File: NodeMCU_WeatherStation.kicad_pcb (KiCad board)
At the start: 2 copper layers, 64 x 90 mm, 98 parts, among them J1 AVR-ISP-6, J10 Screw_Terminal_01x03, J11 Screw_Terminal_01x03, J12 Screw_Terminal_01x02, J13 Screw_Terminal_01x02, J14 Screw_Terminal_01x02, J15 Conn_01x10, J2 Conn_01x15, J3 Conn_01x15, J4 Conn_01x04, J5 Conn_01x04, J6 Conn_01x15, J7 Conn_01x15, J8 Conn_01x07, J9 Screw_Terminal_01x04, U1 BME280, U2 ATmega328P-AU, U3 TLC555CD, U4 ADS122C04IPW, U5 LT1492, U6 LT1492, U7 R-785.0-0.5, Y1 16MHz

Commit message: cleaned up PCB labels
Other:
- board text added: "AVR ISP"
- board text added: "IN1"
- board text added: "IN2"
- board text added: "NodeMCU Weather Station"
- board text added: "OUT1"
- board text added: "OUT2"
- board text added: "RXD"
- board text added: "TXD"
- board text added: "Water Level"
- board text removed: "NodeMCU Wheather Station"
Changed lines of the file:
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@@
   (general
     (thickness 1.6)
-    (drawings 33)
+    (drawings 50)
     (tracks 785)
     (zones 0)
@@
   (page A4)
   (layers
-    (0 F.Cu signal)
-    (31 B.Cu signal)
-    (32 B.Adhes user)
+    (0 F.Cu signal hide)
+    (31 B.Cu signal hide)
+    (32 B.Adhes user hide)
     (33 F.Adhes user)
-    (34 B.Paste user)
+    (34 B.Paste user hide)
     (35 F.Paste user)
-    (36 B.SilkS user)
+    (36 B.SilkS user hide)
     (37 F.SilkS user)
-    (38 B.Mask user)
+    (38 B.Mask user hide)
     (39 F.Mask user)
     (40 Dwgs.User user)
@@
     (44 Edge.Cuts user)
     (45 Margin user)
-    (46 B.CrtYd user)
-    (47 F.CrtYd user)
-    (48 B.Fab user)
-    (49 F.Fab user)
+    (46 B.CrtYd user hide)
+    (47 F.CrtYd user hide)
+    (48 B.Fab user hide)
+    (49 F.Fab user hide)
   )
   (setup
@@
     (descr "terminal block Metz Connect Type055_RT01502HDWU, 2 pins, pitch 5mm, size 10x8mm^2, drill diamater 1.3mm, pad diameter 2.5mm, see http://www.metz-connect.com/de/system/files/productfiles/Datenblatt_310551_RT015xxHDWU_OFF-022723S.pdf, script-generated using https://github.com/pointhi/kicad-footprint-generator/scripts/TerminalBlock_MetzConnect")
     (tags "THT terminal block Metz Connect Type055_RT01502HDWU pitch 5mm size 10x8mm^2 drill 1.3mm pad 2.5mm")
-    (fp_text reference J14 (at 2.5 -5.06 90) (layer F.SilkS)
+    (fp_text reference J14 (at -3.81 2.794 180) (layer F.SilkS)
       (effects (font (size 1 1) (thickness 0.15)))
     )
@@
     (descr "DCDC-Converter, RECOM, RECOM_R-78E-0.5, SIP-3, pitch 2.54mm, package size 11.6x8.5x10.4mm^3, https://www.recom-power.com/pdf/Innoline/R-78Exx-0.5.pdf")
     (tags "dc-dc recom buck sip-3 pitch 2.54mm")
-    (fp_text reference U7 (at 2.54 -7.56 90) (layer F.SilkS)
+    (fp_text reference U7 (at -4.1656 -0.3556) (layer F.SilkS)
       (effects (font (size 1 1) (thickness 0.15)))
     )
@@
     (descr "PhotoDiode, plastic DIL, 4.3x4.65mm², RM5.08")
     (tags "PhotoDiode plastic DIL RM5.08")
-    (fp_text reference D7 (at 2.54 -3.17 90) (layer F.SilkS)
+    (fp_text reference D7 (at -0.8128 2.1336 180) (layer F.SilkS)
       (effects (font (size 1 1) (thickness 0.15)))
     )
@@
     (descr "Through hole straight IDC box header, 2x03, 2.54mm pitch, double rows")
     (tags "Through hole IDC box header THT 2x03 2.54mm double row")
-    (fp_text reference J1 (at 1.27 -6.604) (layer F.SilkS)
+    (fp_text reference J1 (at 1.27 -6.604) (layer F.SilkS) hide
       (effects (font (size 1 1) (thickness 0.15)))
     )
@@
     (tags "mounting hole 4.3mm m4")
     (attr virtual)
-    (fp_text reference H5 (at 0 -5.3) (layer F.SilkS)
+    (fp_text reference H5 (at 0 -5.3) (layer F.SilkS) hide
       (effects (font (size 1 1) (thickness 0.15)))
     )
-    (fp_text value MountingHole_Pad (at 0 5.3) (layer F.Fab)
+    (fp_text value MountingHole_Pad (at 0 5.3) (layer F.Fab) hide
       (effects (font (size 1 1) (thickness 0.15)))
     )
     (fp_circle (center 0 0) (end 4.55 0) (layer F.CrtYd) (width 0.05))
     (fp_circle (center 0 0) (end 4.3 0) (layer Cmts.User) (width 0.15))
-    (fp_text user %R (at 0.3 0) (layer F.Fab)
+    (fp_text user %R (at 0.3 0) (layer F.Fab) hide
       (effects (font (size 1 1) (thickness 0.15)))
     )
@@
     (tags "mounting hole 4.3mm m4")
     (attr virtual)
-    (fp_text reference H4 (at 0 -5.3) (layer F.SilkS)
+    (fp_text reference H4 (at 0 -5.3) (layer F.SilkS) hide
       (effects (font (size 1 1) (thickness 0.15)))
     )
-    (fp_text value MountingHole_Pad (at 0 5.3) (layer F.Fab)
+    (fp_text value MountingHole_Pad (at 0 5.3) (layer F.Fab) hide
       (effects (font (size 1 1) (thickness 0.15)))
     )
     (fp_circle (center 0 0) (end 4.55 0) (layer F.CrtYd) (width 0.05))
     (fp_circle (center 0 0) (end 4.3 0) (layer Cmts.User) (width 0.15))
-    (fp_text user %R (at 0.3 0) (layer F.Fab)
+    (fp_text user %R (at 0.3 0) (layer F.Fab) hide
       (effects (font (size 1 1) (thickness 0.15)))
     )
@@
     (tags "mounting hole 4.3mm m4")
     (attr virtual)
-    (fp_text reference H2 (at 5.1308 -3.386) (layer F.SilkS)
+    (fp_text reference H2 (at 5.1308 -3.386) (layer F.SilkS) hide
       (effects (font (size 1 1) (thickness 0.15)))
     )
-    (fp_text value MountingHole_Pad (at 0 5.3) (layer F.Fab)
+    (fp_text value MountingHole_Pad (at 0 5.3) (layer F.Fab) hide
       (effects (font (size 1 1) (thickness 0.15)))
     )
-    (fp_text user %R (at 0.3 0) (layer F.Fab)
+    (fp_text user %R (at 0.3 0) (layer F.Fab) hide
       (effects (font (size 1 1) (thickness 0.15)))
     )
@@
     (tags "mounting hole 4.3mm m4")
     (attr virtual)
-    (fp_text reference H1 (at -5.09 -3.386) (layer F.SilkS)
+    (fp_text reference H1 (at -5.09 -3.386) (layer F.SilkS) hide
       (effects (font (size 1 1) (thickness 0.15)))
     )
-    (fp_text value MountingHole_Pad (at 0 5.3) (layer F.Fab)
+    (fp_text value MountingHole_Pad (at 0 5.3) (layer F.Fab) hide
       (effects (font (size 1 1) (thickness 0.15)))
     )
-    (fp_text user %R (at 0.3 0) (layer F.Fab)
+    (fp_text user %R (at 0.3 0) (layer F.Fab) hide
       (effects (font (size 1 1) (thickness 0.15)))
     )
@@
     )
   )
+  (gr_text "Water Level" (at 86.8504 140.6552) (layer F.SilkS)
+    (effects (font (size 1 1) (thickness 0.15)))
+  )
+  (gr_text +5V (at 119.464 63.0328) (layer F.SilkS)
+    (effects (font (size 1 1) (thickness 0.15)))
+  )
+  (gr_text GND (at 119.6164 58.1052) (layer F.SilkS)
+    (effects (font (size 1 1) (thickness 0.15)))
+  )
+  (gr_text "AVR ISP" (at 111.0312 140.9092) (layer F.SilkS)
+    (effects (font (size 1 1) (thickness 0.15)))
+  )
+  (gr_text GND (at 124.039181 85.4356) (layer F.SilkS)
+    (effects (font (size 1 1) (thickness 0.15)))
+  )
+  (gr_text RXD (at 124.0868 80.4572) (layer F.SilkS)
+    (effects (font (size 1 1) (thickness 0.15)))
+  )
+  (gr_text OUT1 (at 123.756648 124.2976) (layer F.SilkS)
+    (effects (font (size 1 1) (thickness 0.15)))
+  )
+  (gr_text OUT2 (at 123.756648 119.2176) (layer F.SilkS)
+    (effects (font (size 1 1) (thickness 0.15)))
+  )
+  (gr_text IN1 (at 124.423315 114.1376) (layer F.SilkS)
+    (effects (font (size 1 1) (thickness 0.15)))
+  )
+  (gr_text IN2 (at 124.423315 109.0576) (layer F.SilkS)
+    (effects (font (size 1 1) (thickness 0.15)))
+  )
+  (gr_text GND (at 124.1376 121.7576) (layer F.SilkS)
+    (effects (font (size 1 1) (thickness 0.15)))
+  )
+  (gr_text GND (at 124.1376 116.6776) (layer F.SilkS)
+    (effects (font (size 1 1) (thickness 0.15)))
+  )
+  (gr_text GND (at 124.1376 111.5976) (layer F.SilkS)
+    (effects (font (size 1 1) (thickness 0.15)))
+  )
+  (gr_text GND (at 124.1376 106.5176) (layer F.SilkS)
+    (effects (font (size 1 1) (thickness 0.15)))
+  )
+  (gr_text +5V (at 124.1376 103.9776) (layer F.SilkS)
+    (effects (font (size 1 1) (thickness 0.15)))
+  )
+  (gr_text +5V (at 124.1376 101.4376) (layer F.SilkS)
+    (effects (font (size 1 1) (thickness 0.15)))
+  )
+  (gr_text TXD (at 124.205848 82.9464) (layer F.SilkS)
+    (effects (font (size 1 1) (thickness 0.15)))
+  )
   (gr_text PT100 (at 76.9444 48.3516) (layer Dwgs.User)
     (effects (font (size 1 1) (thickness 0.15)))
@@
     (effects (font (size 1.5 1.5) (thickness 0.25)))
   )
-  (gr_text "NodeMCU Wheather Station" (at 126.6776 113.3248 90) (layer F.SilkS)
+  (gr_text "NodeMCU Weather Station" (at 120.6832 111.9024 90) (layer F.SilkS)
     (effects (font (size 1.5 1.5) (thickness 0.25)))
   )

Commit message: changed to 3.2mm holes for mounting the PCB
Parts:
- H3, H4, H5, H6: footprint MountingHole:MountingHole_4.3mm_M4_Pad_Via -> MountingHole:MountingHole_3.2mm_M3_Pad_Via

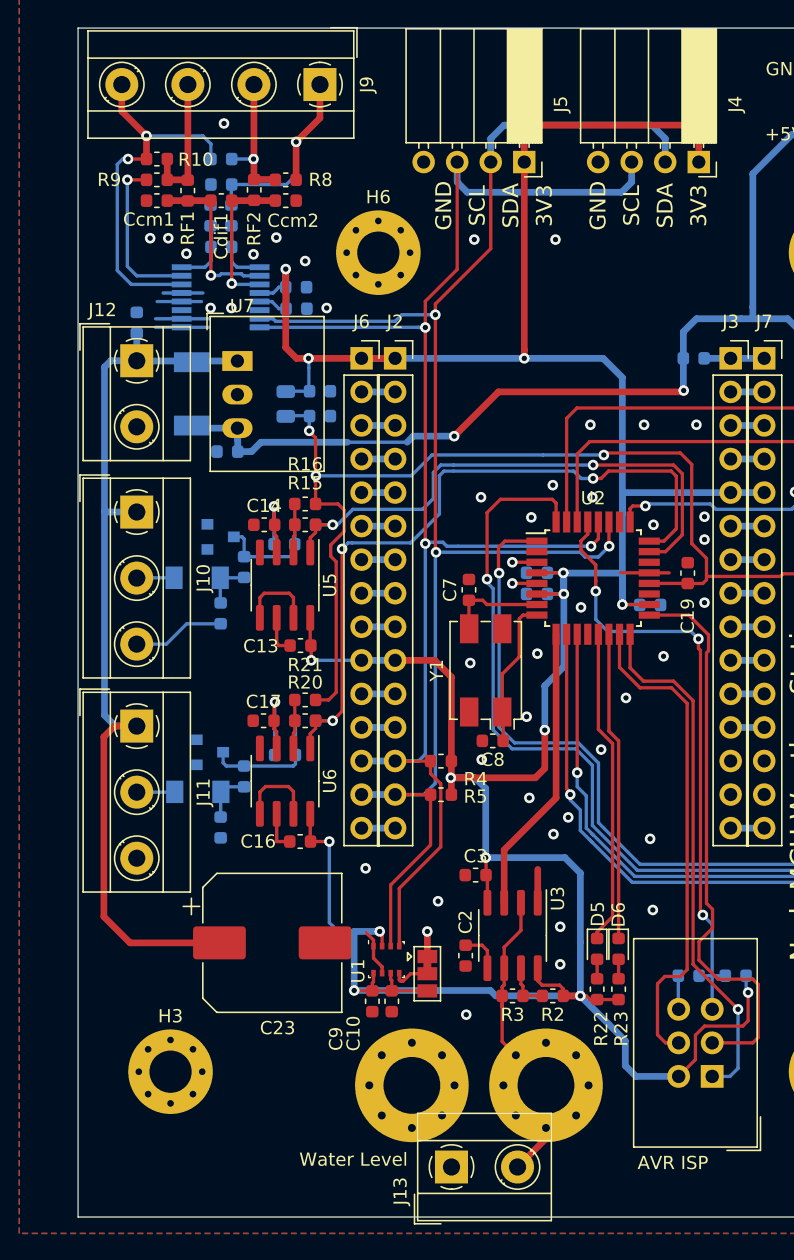
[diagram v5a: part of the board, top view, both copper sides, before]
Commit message: added proper reset to PT100 readout
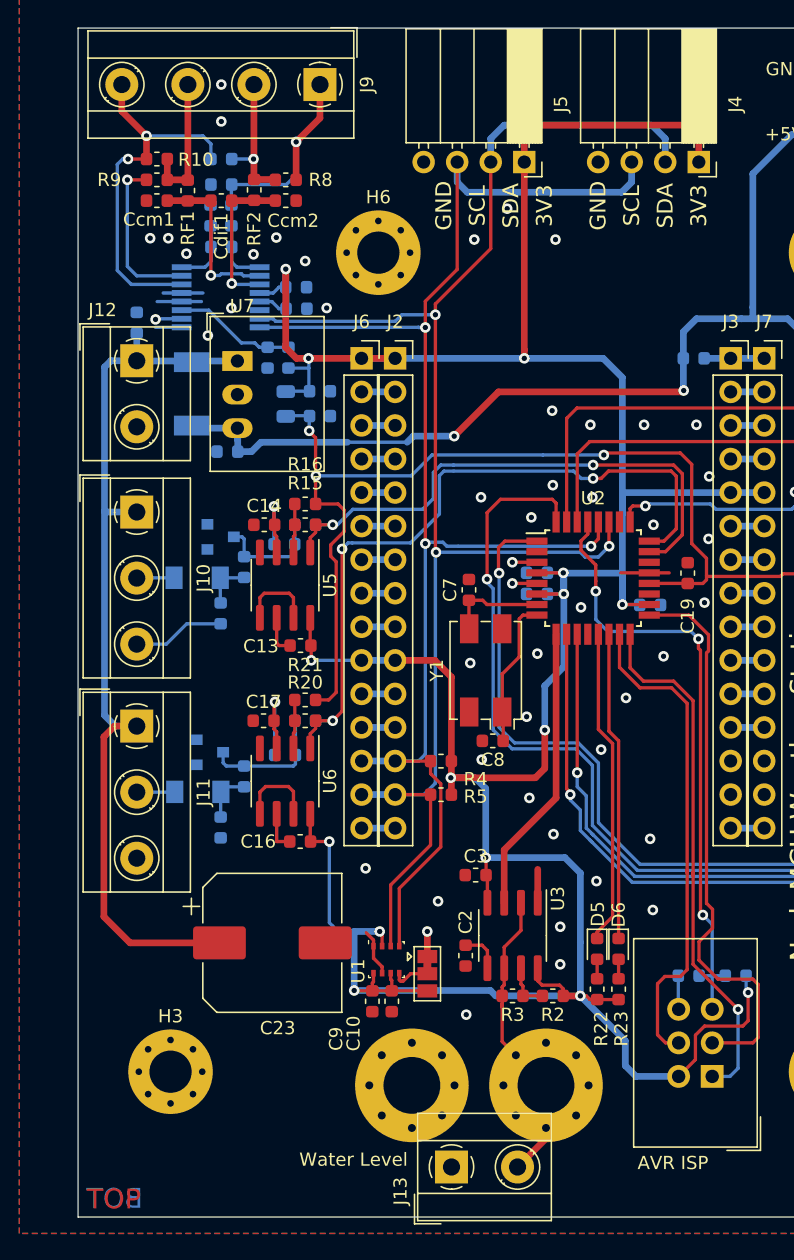
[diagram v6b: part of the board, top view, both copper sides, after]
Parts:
- added C26: 100n, Capacitor_SMD:C_0603_1608Metric, B.Cu at (80.3, 79.9)
- added R26: 10k, Resistor_SMD:R_0603_1608Metric, B.Cu at (81.9, 79.9)
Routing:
- net Net-(C26-Pad1): track 0.00 -> 9.24 mm
- net GND: track 55.8 -> 51.7 mm, vias 49 -> 53
- net +3V3: track 277.3 -> 278.9 mm
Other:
- board text added: "BOT"
- board text added: "TOP"

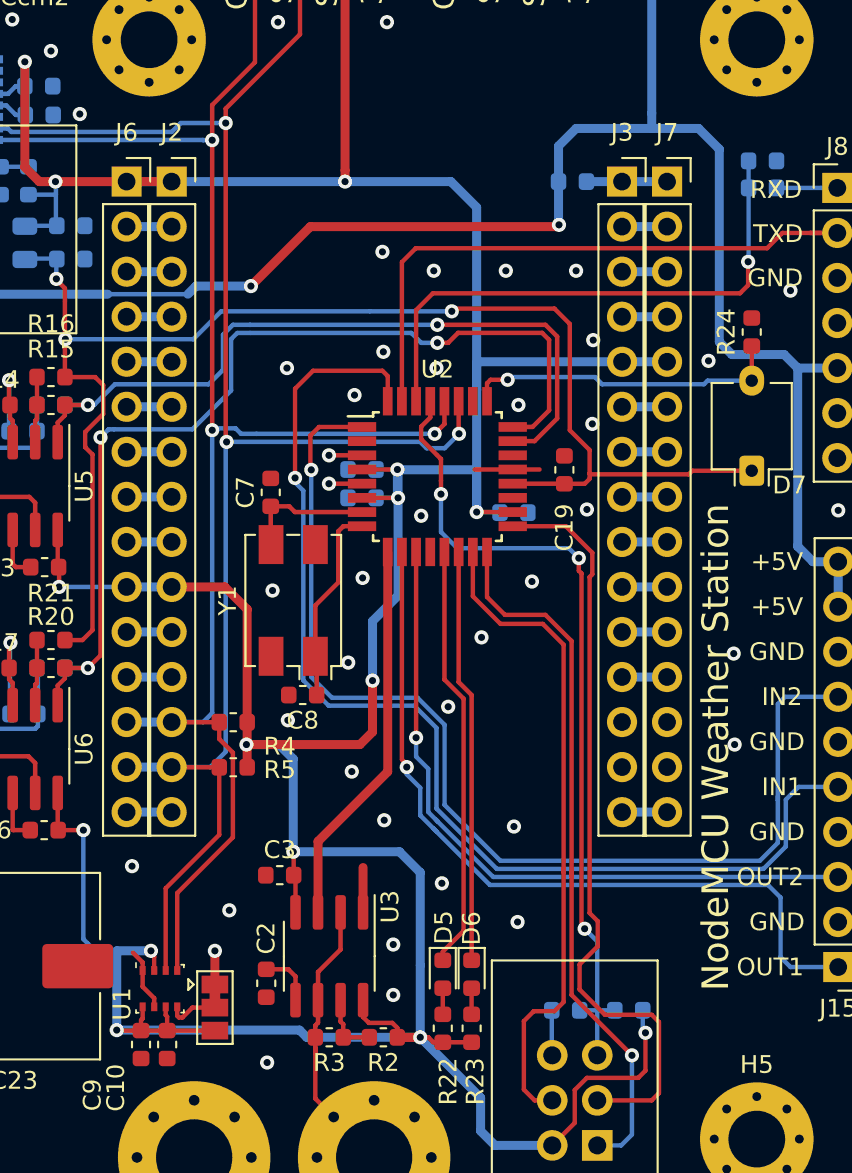
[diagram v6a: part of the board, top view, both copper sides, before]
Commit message: included address jumper for AVR, which makes it easier to use multiple of these boards at the same I2C bus.
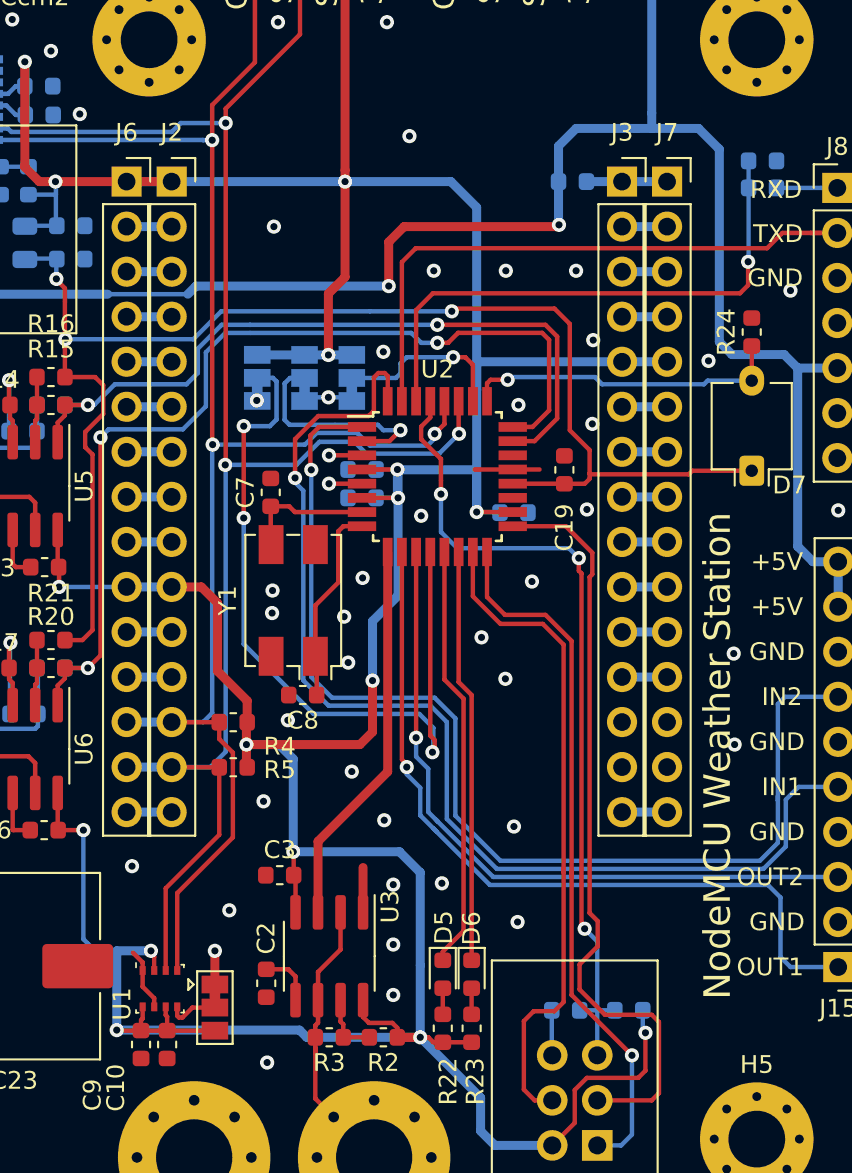
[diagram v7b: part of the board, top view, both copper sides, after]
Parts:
- added JP2: SolderJumper_3_Bridged12, Jumper:SolderJumper-3_P1.3mm_Bridged12_Pad1.0x1.5mm, B.Cu at (94.8, 91.1)
- added JP3: SolderJumper_3_Bridged12, Jumper:SolderJumper-3_P1.3mm_Bridged12_Pad1.0x1.5mm, B.Cu at (100.2, 91.1)
- added JP4: SolderJumper_3_Bridged12, Jumper:SolderJumper-3_P1.3mm_Bridged12_Pad1.0x1.5mm, B.Cu at (97.5, 91.1)
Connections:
- U2 pad 12: Net-(U2-Pad12) -> /I2C Water Sensor/ADDR0
- U2 pad 2: Net-(U2-Pad2) -> /I2C Water Sensor/ADDR2
- U2 pad 26: /I2C Water Sensor/ADC3 -> /I2C Water Sensor/ADDR1
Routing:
- net /I2C Water Sensor/ADDR0: track 0.00 -> 42.8 mm, vias 0 -> 3
- net +3V3: track 278.9 -> 293.3 mm, vias 15 -> 16
- net /I2C Water Sensor/ADDR2: track 0.00 -> 13.9 mm, vias 0 -> 1
- net /I2C Water Sensor/ADDR1: track 0.00 -> 9.87 mm, vias 0 -> 1
- net GND: track 51.7 -> 54.5 mm, vias 53 -> 57
- net +5V: track 110.3 -> 111.8 mm
- net /SDA: track 116.8 -> 117.6 mm
- net /SCL: track 113.4 -> 114.2 mm
- net /I2C Water Sensor/DigIn2: track 62.1 -> 62.6 mm

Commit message: include latest changes
latest changes to design
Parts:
- removed H1, H2: MountingHole_Pad, MountingHole:MountingHole_4.3mm_M4_Pad_Via
- added J16: Conn_01x02, Connector_PinHeader_2.54mm:PinHeader_1x02_P2.54mm_Vertical, F.Cu at (234.9, 103.5)
- C19, C2, C3, R2, R24, R3, U3: moved to B.Cu
- moved C5 229.0 mm to (317.9, 23.5)
- moved C6 229.0 mm to (317.9, 25.1)
- moved C8 229.0 mm to (314.6, 36.3)
- moved JP4 229.0 mm to (314.7, 18.4)
- moved R25 229.0 mm to (329.8, 7.31)
- moved R4 229.0 mm to (310.6, 37.8)
- moved R5 229.0 mm to (310.6, 40.3)
- moved U2 229.0 mm to (322.2, 23.9)
- moved Y1 229.0 mm to (314.0, 30.9)
- moved C4 229.0 mm to (326.5, 26.0)
- moved C7 229.0 mm to (312.8, 24.8)
- moved JP2 229.0 mm to (312.0, 18.4)
- moved JP3 229.0 mm to (317.3, 18.4)
- moved C19 227.7 mm to (328.0, 23.6)
- moved R24 146.7 mm to (251.9, 19.0)
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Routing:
- net +3V3: track 293.3 -> 258.6 mm, vias 16 -> 17
- net /SCL: track 114.2 -> 90.5 mm
- net /SDA: track 117.6 -> 96.1 mm
- net /I2C Water Sensor/TXD: track 33.7 -> 13.9 mm
- net /I2C Water Sensor/DigOut2: track 39.8 -> 20.3 mm
- net /I2C Water Sensor/RXD: track 31.5 -> 14.1 mm
- net +5V: track 111.8 -> 94.6 mm
- net /I2C Water Sensor/DigOut1: track 44.6 -> 28.9 mm
- net /I2C Water Sensor/DigIn1: track 64.4 -> 49.4 mm
- net /I2C Water Sensor/DigIn2: track 62.6 -> 48.0 mm
- net /Sensor Front End/THR: track 23.1 -> 8.73 mm
- net /I2C Water Sensor/ADC2: track 18.3 -> 13.6 mm
- net /I2C Water Sensor/FREQIN: track 22.0 -> 22.9 mm
- net /4to20in 1/Vref: track 79.6 -> 79.3 mm, vias 3 -> 4
- net GND: vias 57 -> 58
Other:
- board size 64 x 90 mm -> 54.1 x 104.1 mm
